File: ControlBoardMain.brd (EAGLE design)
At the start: 65 x 30 mm, 11 parts, among them J1 350759-4, J2 RPI_HEADER, J3 DC_POWERJACK, J4 22-23-2021, Q1 NMOS, U1 VOLTAGE_REGULATOR

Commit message: Added flyback diode
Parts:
- added D1: DIODE, 00_ThruHole:TH_PASSIVE
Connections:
- net GND: now also D1.P2
- net PUMP_GND: now also D1.P1
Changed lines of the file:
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@@
 <grid distance="0.5" unitdist="mm" unit="mm" style="lines" multiple="1" display="yes" altdistance="1" altunitdist="mm" altunit="mm"/>
 <layers>
-<layer number="1" name="Top" color="4" fill="1" visible="yes" active="yes"/>
+<layer number="1" name="Top" color="4" fill="1" visible="no" active="yes"/>
 <layer number="2" name="Route2" color="1" fill="3" visible="no" active="no"/>
 <layer number="15" name="Route15" color="4" fill="6" visible="no" active="no"/>
@@
 </element>
 <element name="U$1" library="1111Lib" package="LOGO" value="LOGO" x="29" y="21"/>
+<element name="D1" library="00_ThruHole" package="TH_PASSIVE" value="DIODE" x="59" y="8" rot="R90"/>
 </elements>
 <signals>
@@
 <vertex x="3.5" y="3.5"/>
 </polygon>
+<contactref element="D1" pad="P2"/>
 </signal>
 <signal name="5V_RPI">
@@
 <contactref element="Q1" pad="P2"/>
 <contactref element="J1" pad="1"/>
-<polygon width="0.2" layer="16">
-<vertex x="55" y="11.5"/>
+<contactref element="D1" pad="P1"/>
+<polygon width="0.4064" layer="16">
+<vertex x="34.5" y="3"/>
+<vertex x="61.5" y="3"/>
+<vertex x="61.5" y="11.5"/>
 <vertex x="48" y="11.5"/>
 <vertex x="48" y="16"/>
 <vertex x="34.5" y="16"/>
-<vertex x="34.5" y="3"/>
-<vertex x="55" y="3"/>
 </polygon>
 </signal>

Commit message: Fixed the flyback diode
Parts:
- moved D1 10.0 mm to (59.0, 18.0), turned to 270 degrees
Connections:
- net GND: no longer D1.P2
- net PUMP_GND: now also D1.P2; no longer D1.P1
- net VIN: now also D1.P1
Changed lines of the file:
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@@
 </element>
 <element name="U$1" library="1111Lib" package="LOGO" value="LOGO" x="29" y="21"/>
-<element name="D1" library="00_ThruHole" package="TH_PASSIVE" value="DIODE" x="59" y="8" rot="R90"/>
+<element name="D1" library="00_ThruHole" package="TH_PASSIVE" value="DIODE" x="59" y="18" rot="R270"/>
 </elements>
 <signals>
@@
 <vertex x="3.5" y="3.5"/>
 </polygon>
-<contactref element="D1" pad="P2"/>
 </signal>
 <signal name="5V_RPI">
@@
 <contactref element="Q1" pad="P2"/>
 <contactref element="J1" pad="1"/>
-<contactref element="D1" pad="P1"/>
 <polygon width="0.4064" layer="16">
 <vertex x="34.5" y="3"/>
@@
 <vertex x="34.5" y="16"/>
 </polygon>
+<contactref element="D1" pad="P2"/>
 </signal>
 <signal name="PUMP_ON">
@@
 <contactref element="R2" pad="P1"/>
 <contactref element="J1" pad="2"/>
-<polygon width="0.2" layer="16">
-<vertex x="3.5" y="3"/>
-<vertex x="34" y="3"/>
-<vertex x="34" y="16.5"/>
-<vertex x="48.5" y="16.5"/>
-<vertex x="48.5" y="12"/>
-<vertex x="54.5" y="12"/>
-<vertex x="54.5" y="22"/>
-<vertex x="3.5" y="22"/>
+<contactref element="D1" pad="P1"/>
+<polygon width="0.4064" layer="16">
+<vertex x="49" y="12.5"/>
+<vertex x="61.5" y="12.5"/>
+<vertex x="61.5" y="22"/>
+<vertex x="2" y="22"/>
+<vertex x="2" y="3.5"/>
+<vertex x="2" y="3"/>
+<vertex x="33.5" y="3"/>
+<vertex x="33.5" y="17"/>
+<vertex x="49" y="17"/>
 </polygon>
 </signal>

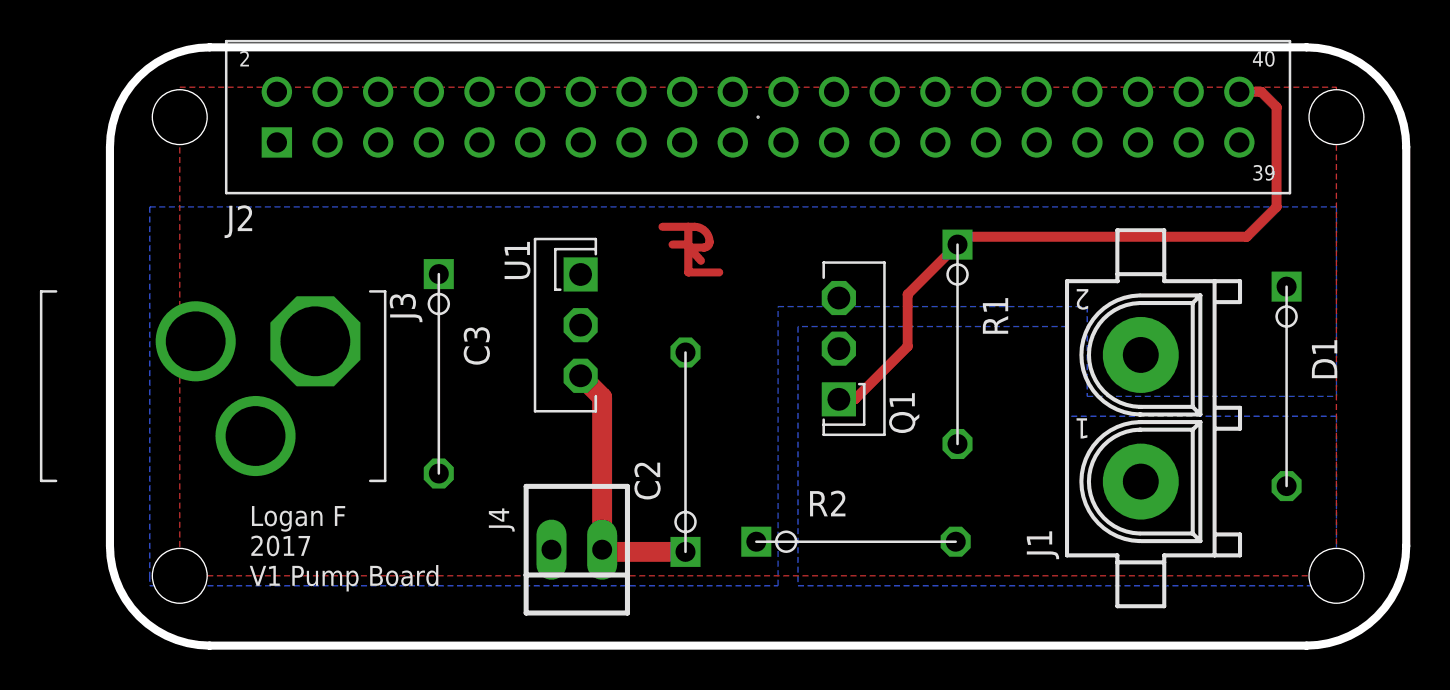
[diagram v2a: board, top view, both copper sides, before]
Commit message: Updated .gitignore and various other docs
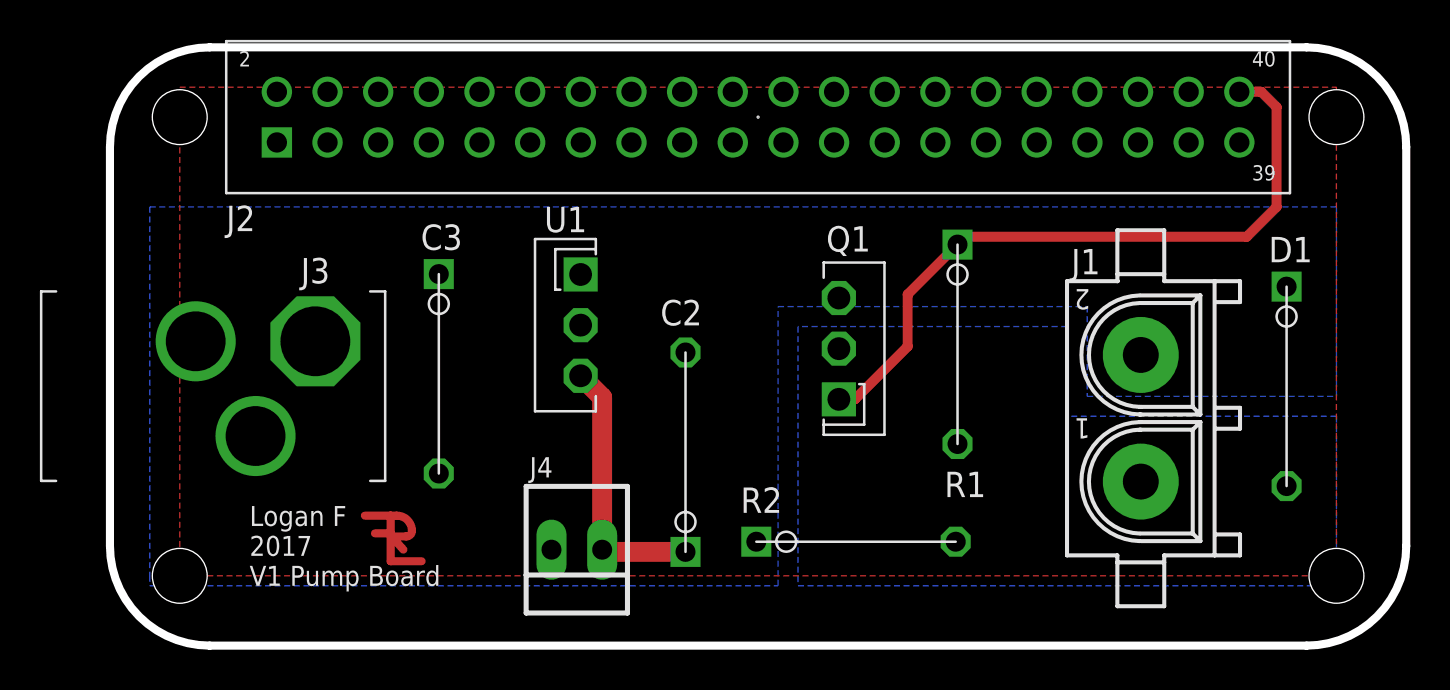
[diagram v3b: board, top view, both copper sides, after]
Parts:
- moved U$1 20.8 mm to (14.1, 6.52)
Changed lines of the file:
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@@
 <setting verticaltext="up"/>
 </settings>
-<grid distance="0.5" unitdist="mm" unit="mm" style="lines" multiple="1" display="yes" altdistance="1" altunitdist="mm" altunit="mm"/>
+<grid distance="1" unitdist="mil" unit="mil" style="lines" multiple="1" display="yes" altdistance="1" altunitdist="mm" altunit="mm"/>
 <layers>
-<layer number="1" name="Top" color="4" fill="1" visible="no" active="yes"/>
+<layer number="1" name="Top" color="4" fill="1" visible="yes" active="yes"/>
 <layer number="2" name="Route2" color="1" fill="3" visible="no" active="no"/>
 <layer number="15" name="Route15" color="4" fill="6" visible="no" active="no"/>
-<layer number="16" name="Bottom" color="1" fill="1" visible="yes" active="yes"/>
+<layer number="16" name="Bottom" color="1" fill="1" visible="no" active="yes"/>
 <layer number="17" name="Pads" color="2" fill="1" visible="yes" active="yes"/>
 <layer number="18" name="Vias" color="2" fill="1" visible="yes" active="yes"/>
@@
 </autorouter>
 <elements>
-<element name="C2" library="00_ThruHole" package="TH_PASSIVE" value="10uF" x="28.86" y="4.7" rot="R90"/>
-<element name="C3" library="00_ThruHole" package="TH_PASSIVE" value="10uF" x="16.49" y="18.63" rot="R270"/>
-<element name="J1" library="con-amp" package="350759-4" value="350759-4" x="51.69" y="11.4" rot="R90"/>
+<element name="C2" library="00_ThruHole" package="TH_PASSIVE" value="10uF" x="28.86" y="4.7" smashed="yes" rot="R90">
+<attribute name="NAME" x="29.6916" y="17.3284" size="1.27" layer="25" rot="R180"/>
+</element>
+<element name="C3" library="00_ThruHole" package="TH_PASSIVE" value="10uF" x="16.49" y="18.63" smashed="yes" rot="R270">
+<attribute name="NAME" x="15.5838" y="19.8428" size="1.27" layer="25"/>
+</element>
+<element name="J1" library="con-amp" package="350759-4" value="350759-4" x="51.69" y="11.4" smashed="yes" rot="R90">
+<attribute name="NAME" x="49.6616" y="19.8892" size="1.27" layer="25" rot="R180"/>
+</element>
 <element name="J2" library="00_ThruHole" package="RPIHEADER" value="RPI_HEADER" x="8.37" y="25.23" smashed="yes">
 <attribute name="NAME" x="5.83" y="20.785" size="1.27" layer="25"/>
 </element>
-<element name="J3" library="00_ThruHole" package="DC_POWERJACK" value="DC_POWERJACK" x="10.3" y="15.26" rot="R180"/>
-<element name="Q1" library="00_ThruHole" package="TH_3PIN" value="NMOS" x="36.55" y="12.35" rot="R90"/>
-<element name="R1" library="00_ThruHole" package="TH_PASSIVE" value="10k" x="42.5" y="20.11" rot="R270"/>
-<element name="R2" library="00_ThruHole" package="TH_PASSIVE" value="10k" x="32.41" y="5.21"/>
-<element name="U1" library="00_ThruHole" package="TH_3PIN" value="VOLTAGE_REGULATOR" x="23.6" y="18.61" rot="R270"/>
+<element name="J3" library="00_ThruHole" package="DC_POWERJACK" value="DC_POWERJACK" x="10.3" y="15.26" smashed="yes" rot="R180">
+<attribute name="NAME" x="9.5704" y="18.1648" size="1.27" layer="25"/>
+</element>
+<element name="Q1" library="00_ThruHole" package="TH_3PIN" value="NMOS" x="36.55" y="12.35" smashed="yes" rot="R90">
+<attribute name="NAME" x="38.1452" y="21.0306" size="1.27" layer="25" rot="R180"/>
+</element>
+<element name="R1" library="00_ThruHole" package="TH_PASSIVE" value="10k" x="42.5" y="20.11" smashed="yes" rot="R270">
+<attribute name="NAME" x="41.8406" y="7.448" size="1.27" layer="25"/>
+</element>
+<element name="R2" library="00_ThruHole" package="TH_PASSIVE" value="10k" x="32.41" y="5.21" smashed="yes">
+<attribute name="NAME" x="31.6226" y="6.6578" size="1.27" layer="25"/>
+</element>
+<element name="U1" library="00_ThruHole" package="TH_3PIN" value="VOLTAGE_REGULATOR" x="23.6" y="18.61" smashed="yes" rot="R270">
+<attribute name="NAME" x="21.776" y="20.7298" size="1.27" layer="25"/>
+</element>
 <element name="J4" library="con-molex" package="22-23-2021" value="22-23-2021" x="23.41" y="4.81" smashed="yes" rot="R180">
 <attribute name="MF" value="MOLEX" x="23.41" y="4.81" size="1.778" layer="27" rot="R180" display="off"/>
 <attribute name="MPN" value="22-23-2021" x="23.41" y="4.81" size="1.778" layer="27" rot="R180" display="off"/>
-<attribute name="NAME" x="19" y="6.95" size="1.016" layer="25" ratio="10" rot="R270"/>
+<attribute name="NAME" x="21.0408" y="8.4336" size="1.016" layer="25" ratio="10"/>
 <attribute name="OC_FARNELL" value="1462926" x="23.41" y="4.81" size="1.778" layer="27" rot="R180" display="off"/>
 <attribute name="OC_NEWARK" value="25C3832" x="23.41" y="4.81" size="1.778" layer="27" rot="R180" display="off"/>
-<attribute name="VALUE" x="25.95" y="9.89" size="1.016" layer="27" ratio="10" rot="R180"/>
-</element>
-<element name="U$1" library="1111Lib" package="LOGO" value="LOGO" x="29" y="21"/>
-<element name="D1" library="00_ThruHole" package="TH_PASSIVE" value="DIODE" x="59" y="18" rot="R270"/>
+</element>
+<element name="U$1" library="1111Lib" package="LOGO" value="LOGO" x="14.0762" y="6.5174"/>
+<element name="D1" library="00_ThruHole" package="TH_PASSIVE" value="DIODE" x="59" y="18" smashed="yes" rot="R270">
+<attribute name="NAME" x="58.0984" y="19.2236" size="1.27" layer="25"/>
+</element>
 </elements>
 <signals>
